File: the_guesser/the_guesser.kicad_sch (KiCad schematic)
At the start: 20 parts, among them Q1 2N7002, U1 ESP32-S3FN8, U10 TPS61033DRLR, U2 W25Q128JVS, X002 ECS-3953M-400-AU-TR, X2 XRCGB40M000F1S2GR0

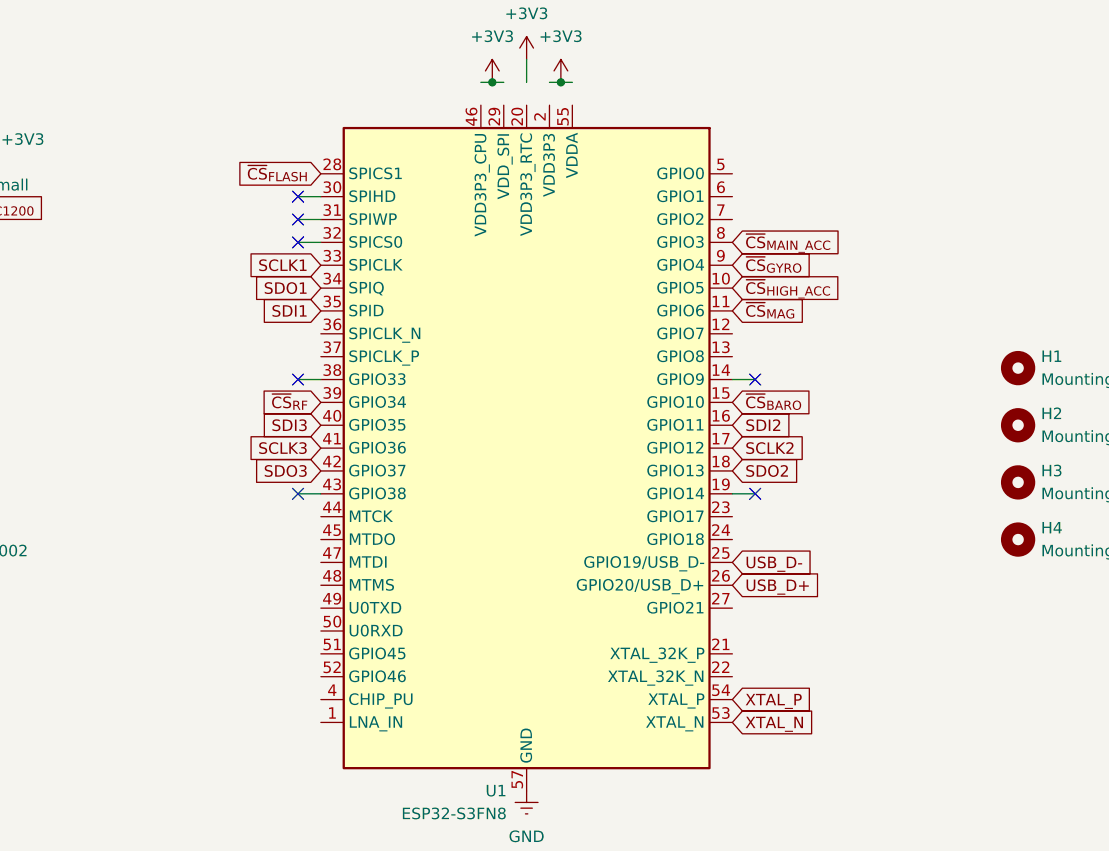
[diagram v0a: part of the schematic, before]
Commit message: Routed USB and SPI buses
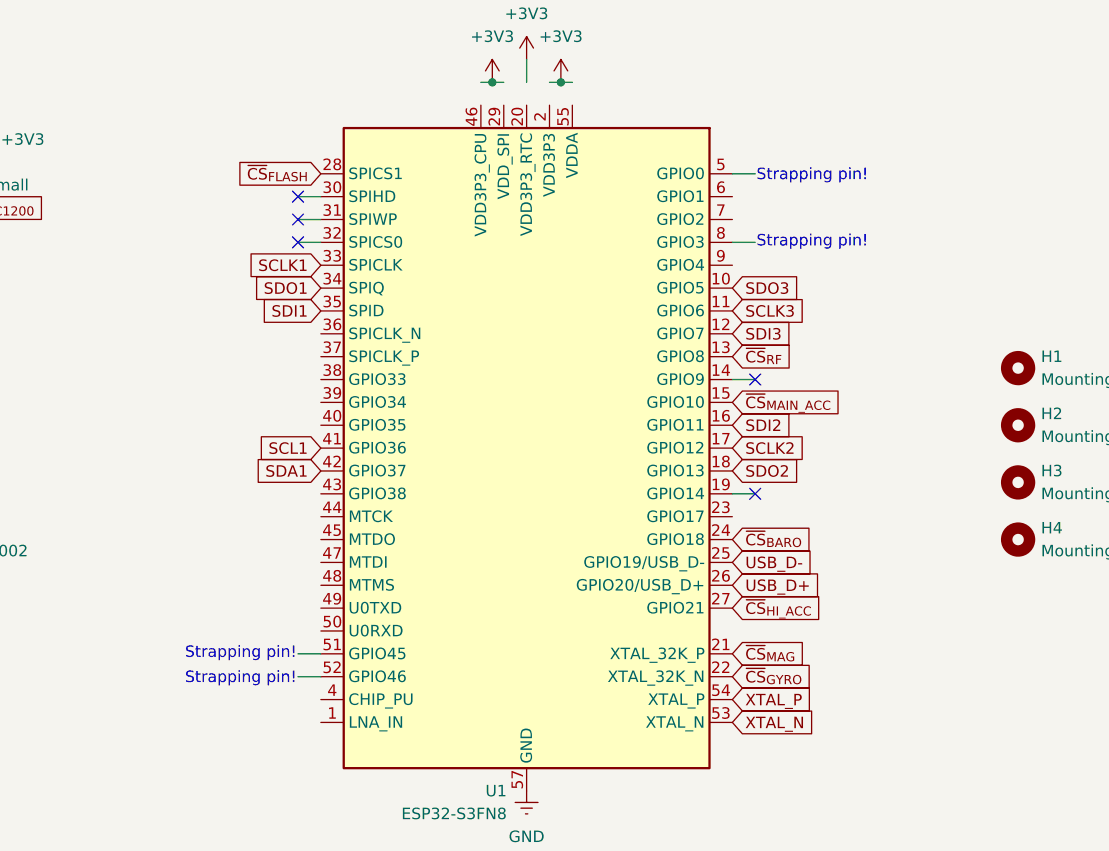
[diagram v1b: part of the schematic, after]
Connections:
- net ~{CS}_{HIGH_ACC} is gone; now on net SDO3: U1.10 (GPIO5)
- net SCLK3: now also U1.11 (GPIO6); no longer U1.41 (GPIO36)
- net SDI3: now also U1.12 (GPIO7); no longer U1.40 (GPIO35)
- net SDO3: no longer U1.42 (GPIO37)
- net ~{CS}_{BARO}: now also U1.24 (GPIO18); no longer U1.15 (GPIO10)
- net ~{CS}_{GYRO}: now also U1.22 (XTAL_32K_N); no longer U1.9 (GPIO4)
- net ~{CS}_{MAG}: now also U1.21 (XTAL_32K_P); no longer U1.11 (GPIO6)
- net ~{CS}_{MAIN_ACC}: now also U1.15 (GPIO10); no longer U1.8 (GPIO3)
- net ~{CS}_{RF}: now also U1.13 (GPIO8); no longer U1.39 (GPIO34)
- net ~{CS}_{HI_ACC}: now reaches U1.27 (GPIO21)
- new net SCL1: U1.41 (GPIO36)
- new net SDA1: U1.42 (GPIO37)
- no-connect marks 7 -> 5
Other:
- note added: "Strapping pin!"

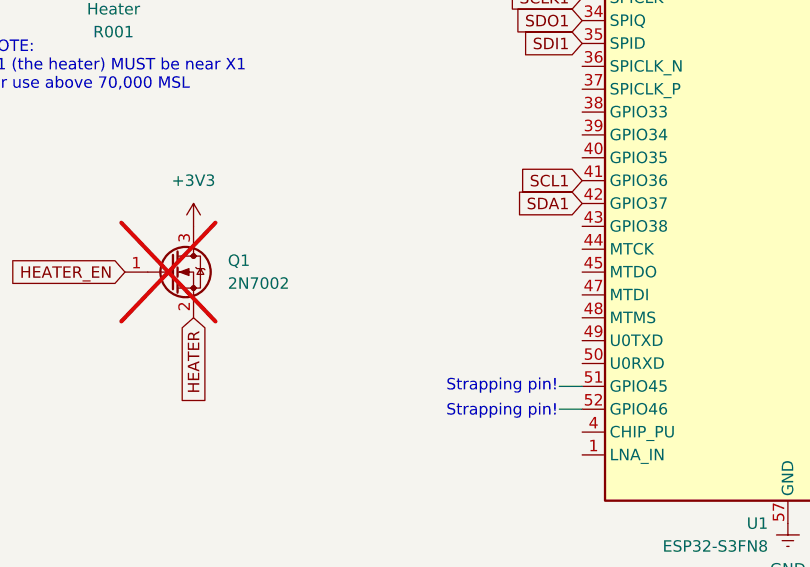
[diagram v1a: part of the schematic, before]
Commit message: Routed Guesser pyro channels
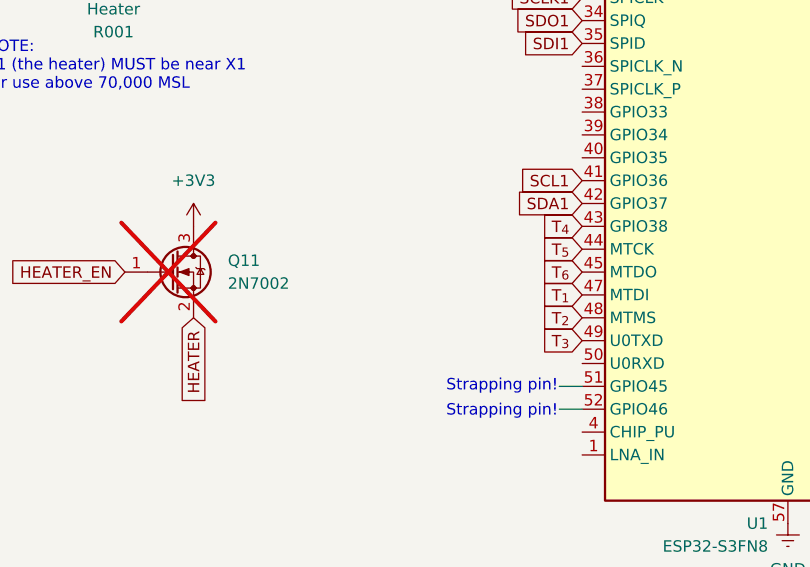
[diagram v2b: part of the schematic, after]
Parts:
- renumbered Q1 to Q11
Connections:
- net T_{4}: now reaches U1.43 (GPIO38)
- net T_{5}: now reaches U1.44 (MTCK)
- net T_{6}: now reaches U1.45 (MTDO)
- net T_{1}: now reaches U1.47 (MTDI)
- net T_{2}: now reaches U1.48 (MTMS)
- net T_{3}: now reaches U1.49 (U0TXD)
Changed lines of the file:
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@@
+		)
+	)
+	(global_label "T_{4}"
+		(shape input)
+		(at 87.63 140.97 180)
+		(fields_autoplaced yes)
+		(effects
+			(font
+				(size 1.27 1.27)
+			)
+			(justify right)
+		)
+		(property "Intersheetrefs" "${INTERSHEET_REFS}"
+			(at 82.6588 140.97 0)
+			(effects
+				(font
+					(size 1.27 1.27)
+				)
+				(justify right)
+				(hide yes)
+			)
+		)
+	)
+	(global_label "T_{1}"
+		(shape input)
+		(at 87.63 148.59 180)
+		(fields_autoplaced yes)
+		(effects
+			(font
+				(size 1.27 1.27)
+			)
+			(justify right)
+		)
+		(property "Intersheetrefs" "${INTERSHEET_REFS}"
+			(at 82.6588 148.59 0)
+			(effects
+				(font
+					(size 1.27 1.27)
+				)
+				(justify right)
+				(hide yes)
+			)
+		)
+	)
+	(global_label "T_{6}"
+		(shape input)
+		(at 87.63 146.05 180)
+		(fields_autoplaced yes)
+		(effects
+			(font
+				(size 1.27 1.27)
+			)
+			(justify right)
+		)
+		(property "Intersheetrefs" "${INTERSHEET_REFS}"
+			(at 82.6588 146.05 0)
+			(effects
+				(font
+					(size 1.27 1.27)
+				)
+				(justify right)
+				(hide yes)
+			)
 		)
 	)
@@
 		)
 	)
+	(global_label "T_{2}"
+		(shape input)
+		(at 87.63 151.13 180)
+		(fields_autoplaced yes)
+		(effects
+			(font
+				(size 1.27 1.27)
+			)
+			(justify right)
+		)
+		(property "Intersheetrefs" "${INTERSHEET_REFS}"
+			(at 82.6588 151.13 0)
+			(effects
+				(font
+					(size 1.27 1.27)
+				)
+				(justify right)
+				(hide yes)
+			)
+		)
+	)
 	(global_label "SCLK1"
 		(shape input)
@@
 		)
 	)
+	(global_label "T_{5}"
+		(shape input)
+		(at 87.63 143.51 180)
+		(fields_autoplaced yes)
+		(effects
+			(font
+				(size 1.27 1.27)
+			)
+			(justify right)
+		)
+		(property "Intersheetrefs" "${INTERSHEET_REFS}"
+			(at 82.6588 143.51 0)
+			(effects
+				(font
+					(size 1.27 1.27)
+				)
+				(justify right)
+				(hide yes)
+			)
+		)
+	)
 	(global_label "~{CS}_{FLASH}"
 		(shape input)
@@
 		(property "Intersheetrefs" "${INTERSHEET_REFS}"
 			(at 79.9277 135.89 0)
+			(effects
+				(font
+					(size 1.27 1.27)
+				)
+				(justify right)
+				(hide yes)
+			)
+		)
+	)
+	(global_label "T_{3}"
+		(shape input)
+		(at 87.63 153.67 180)
+		(fields_autoplaced yes)
+		(effects
+			(font
+				(size 1.27 1.27)
+			)
+			(justify right)
+		)
+		(property "Intersheetrefs" "${INTERSHEET_REFS}"
+			(at 82.6588 153.67 0)
 			(effects
 				(font
@@
 		(dnp yes)
 		(fields_autoplaced yes)
-		(property "Reference" "Q1"
+		(property "Reference" "Q11"
 			(at 48.26 144.7799 0)
 			(effects
@@
 			(project "the_guesser"
 				(path "/473e3a2e-6c5e-4995-af4a-e4bf1449cab0"
-					(reference "Q1")
+					(reference "Q11")
 					(unit 1)
 				)

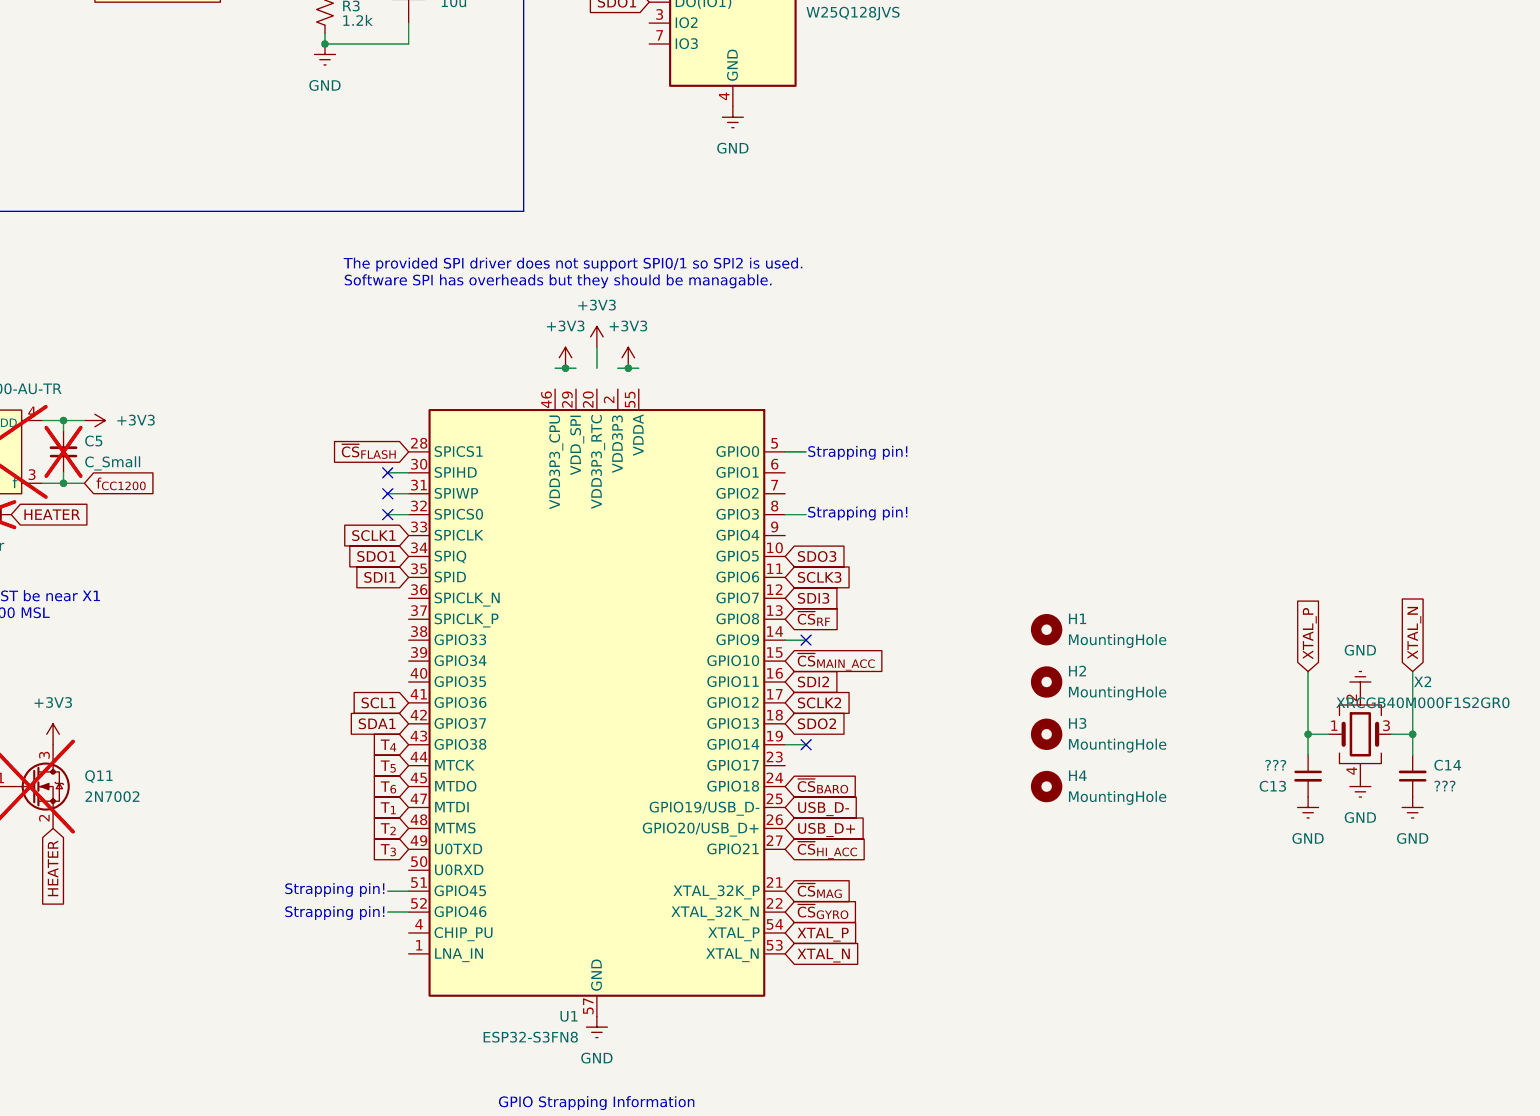
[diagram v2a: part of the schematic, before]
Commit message: Finished routing Guesser
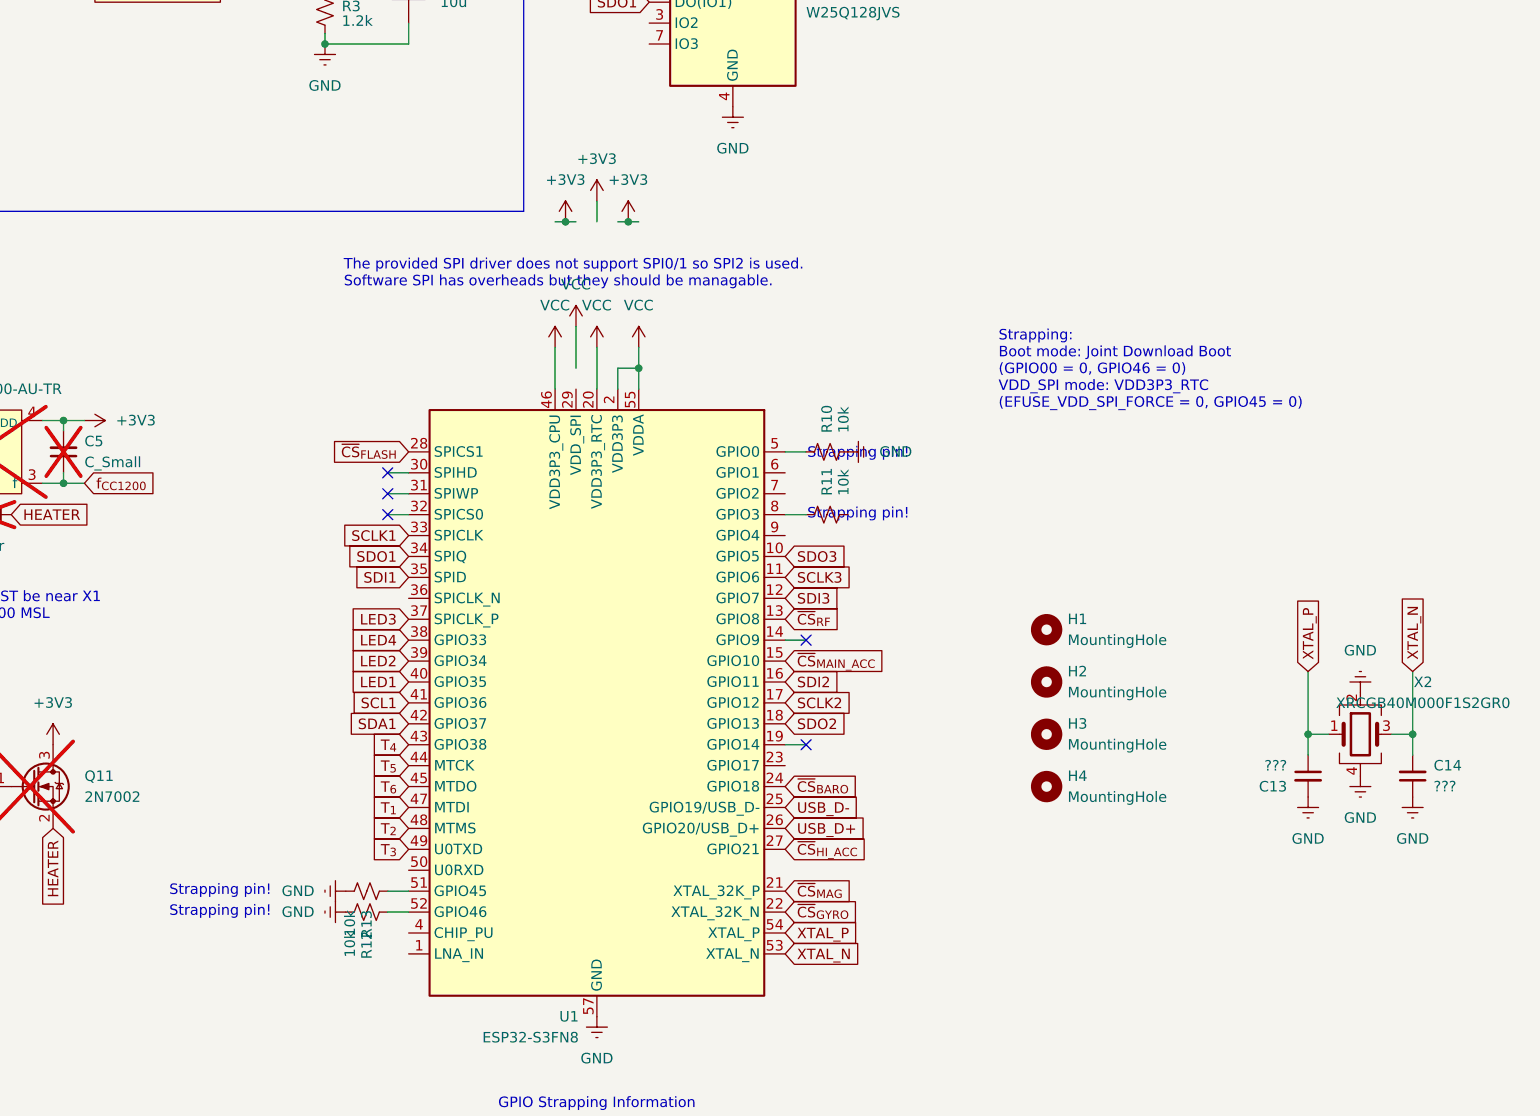
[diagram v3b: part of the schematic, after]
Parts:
- added R10, R11, R12, R13: 10k, Resistor_SMD:R_0603_1608Metric, symbol Device:R_Small_US
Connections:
- net GND: now also R10.2, R12.2, R13.2
- net VCC: now also U1.2 (VDD3P3), U1.20 (VDD3P3_RTC), U1.3 (VDD3P3), U1.46 (VDD3P3_CPU), U1.55 (VDDA), U1.56 (VDDA)
- net LED3: now reaches U1.37 (SPICLK_P)
- net LED4: now reaches U1.38 (GPIO33)
- net LED2: now reaches U1.39 (GPIO34)
- net LED1: now reaches U1.40 (GPIO35)
- net at U1.5 (GPIO0): now also R10.1
- net at U1.51 (GPIO45): now also R13.1
- net at U1.52 (GPIO46): now also R12.1
- net at U1.8 (GPIO3): now also R11.1
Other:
- note added: "Strapping: Boot mode: Joint Download Boot (GPIO00 = 0, GPIO46 = 0) VDD_SPI mode: VDD3P3_RTC (EFUSE_VDD_SPI_FORCE = 0, GPIO45 = 0)"
